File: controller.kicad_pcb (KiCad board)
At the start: 2 copper layers, 26.8 x 31.5 mm, 27 parts, among them J1 Conn_ST_STDC14, P1 USB_C_Plug_USB2.0, SW1 SW_Push, SW2 SW_Push, U1 STM32L476RGTx, U2 BD33FC0FP, U3 NUP2202

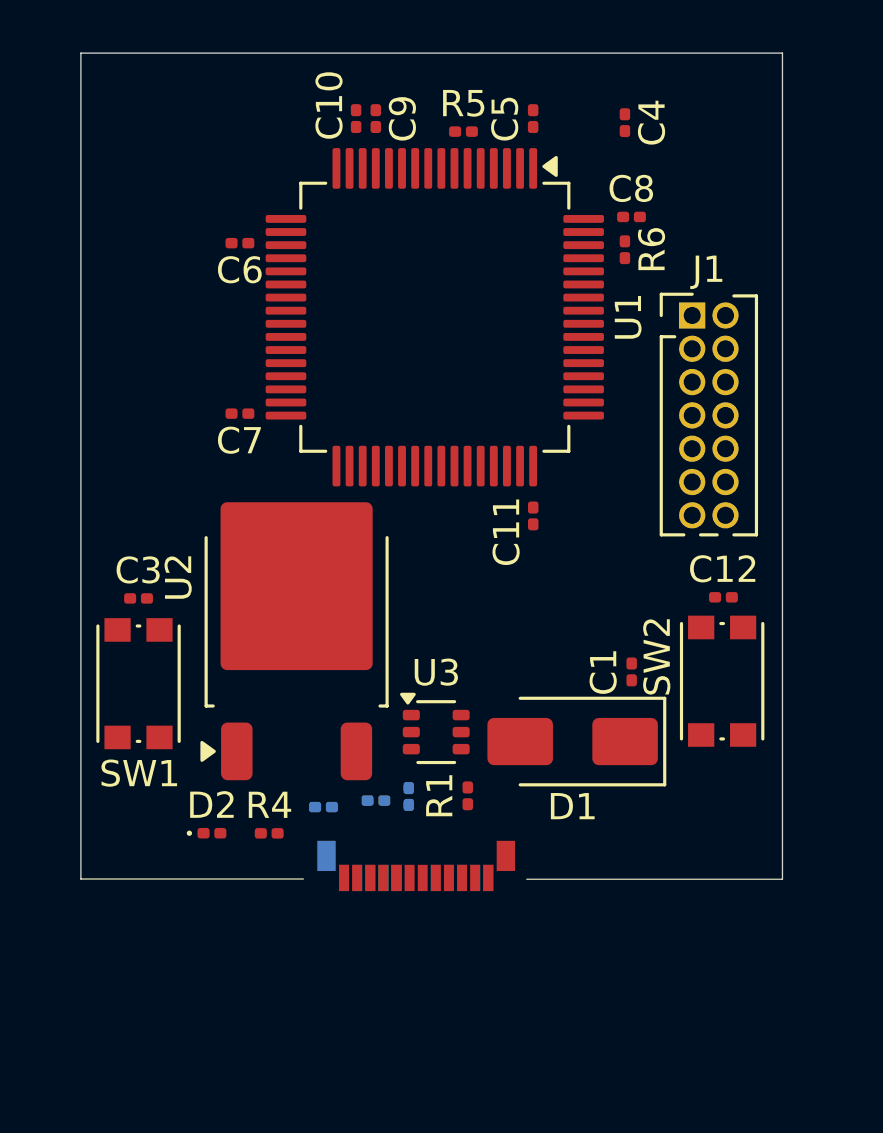
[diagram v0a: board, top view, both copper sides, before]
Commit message: initial ground/power routing
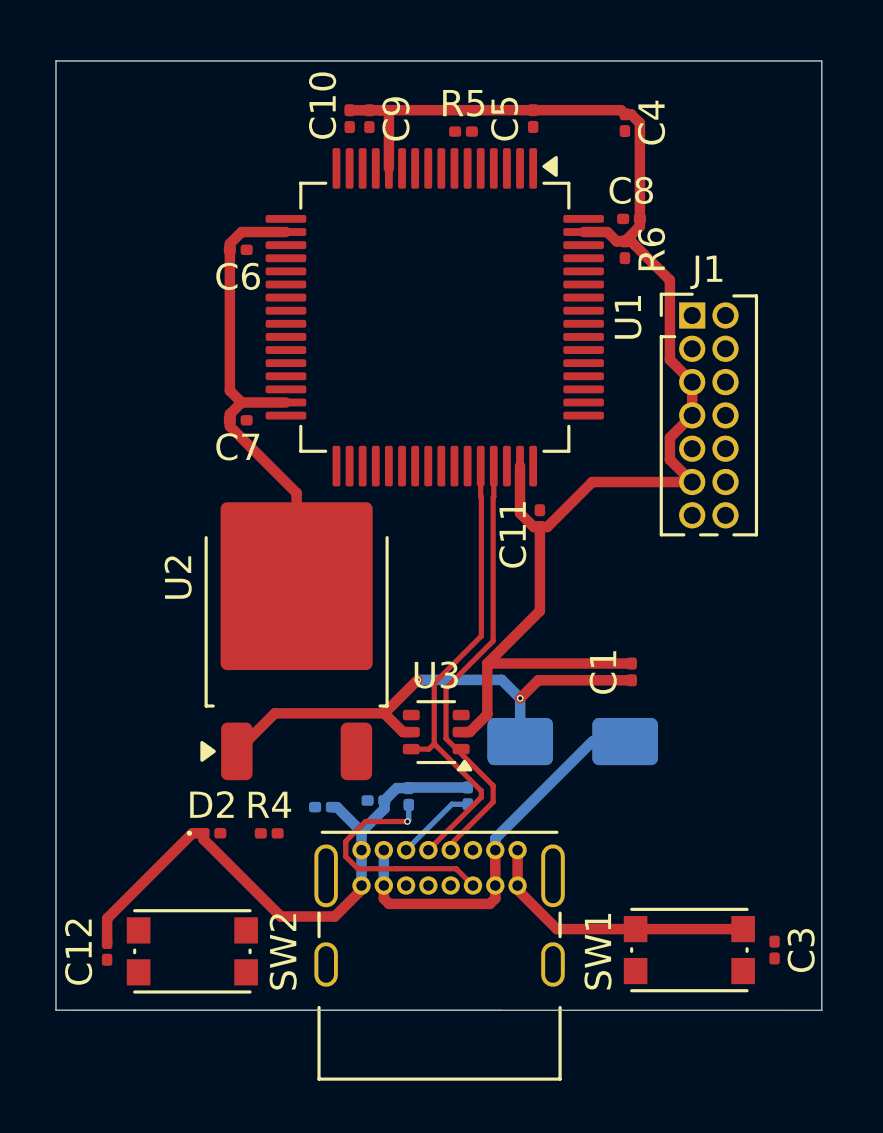
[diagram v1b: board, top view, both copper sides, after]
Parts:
- D1, R1: moved to B.Cu
- P1: footprint Connector_USB:USB_C_Plug_Molex_105444 -> Connector_USB:USB_C_Receptacle_GCT_USB4085
- moved C3 27.7 mm to (89.2, 79.7), turned to -90 degrees
- moved C12 27.1 mm to (63.8, 79.8), turned to 90 degrees
- moved SW1 23.3 mm to (86.0, 79.7), turned to 0 degrees
- moved SW2 22.7 mm to (67.0, 79.8), turned to 0 degrees
- moved P1 2.36 mm to (73.5, 75.9), turned to 0 degrees
- moved C11 0.27 mm to (80.2, 63.2)
- moved C6 0.26 mm to (68.8, 53.0)
- moved C7 0.26 mm to (68.8, 59.5)
- moved C10 0.24 mm to (73.0, 48.0)
- moved C9 0.24 mm to (73.8, 48.0)
- moved C8 0.08 mm to (83.7, 51.8)
- turned D1 to 0 degrees
- turned U3 to 180 degrees
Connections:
- net Net-(D1-A) renamed /VUSB
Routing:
- net GND: track 0.00 -> 106.8 mm
- net +5V: track 0.00 -> 19.7 mm, vias 0 -> 2
- net D+: track 0.00 -> 17.9 mm
- net D-: track 0.00 -> 16.8 mm
- net /VUSB: track 0.00 -> 15.0 mm
- net Net-(P1-VCONN): track 0.00 -> 9.21 mm, vias 0 -> 1
- net Net-(P1-CC): track 0.00 -> 3.07 mm
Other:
- board size 26.8 x 31.5 mm -> 29.2 x 36.2 mm

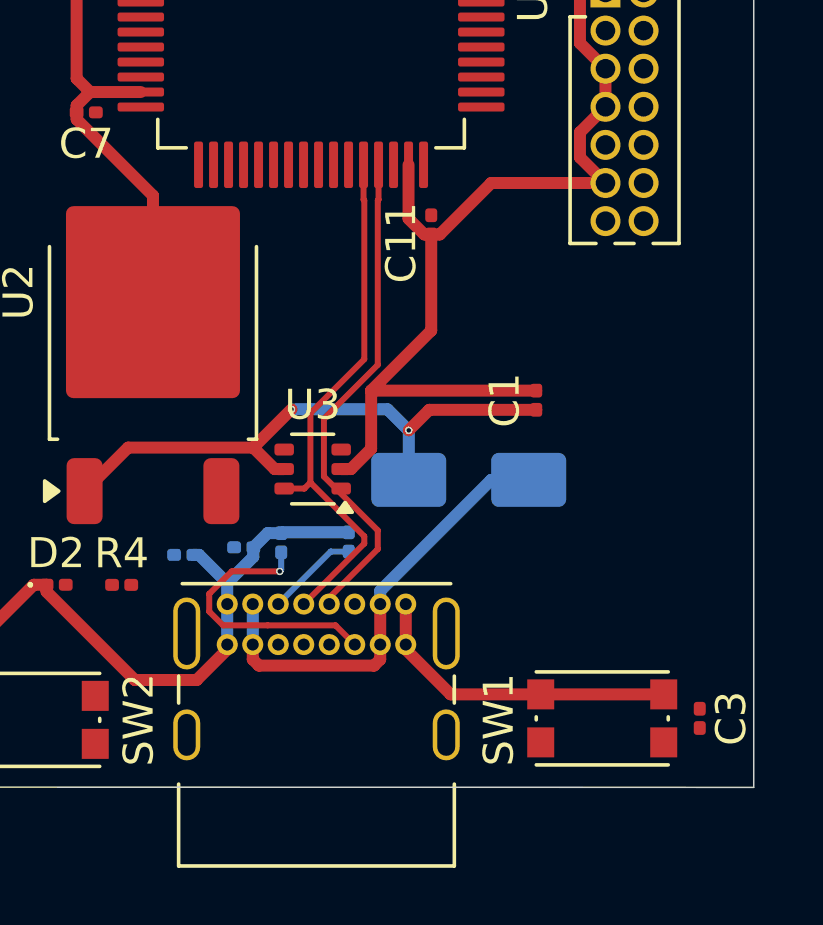
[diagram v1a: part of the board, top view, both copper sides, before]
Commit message: a bit more power routing
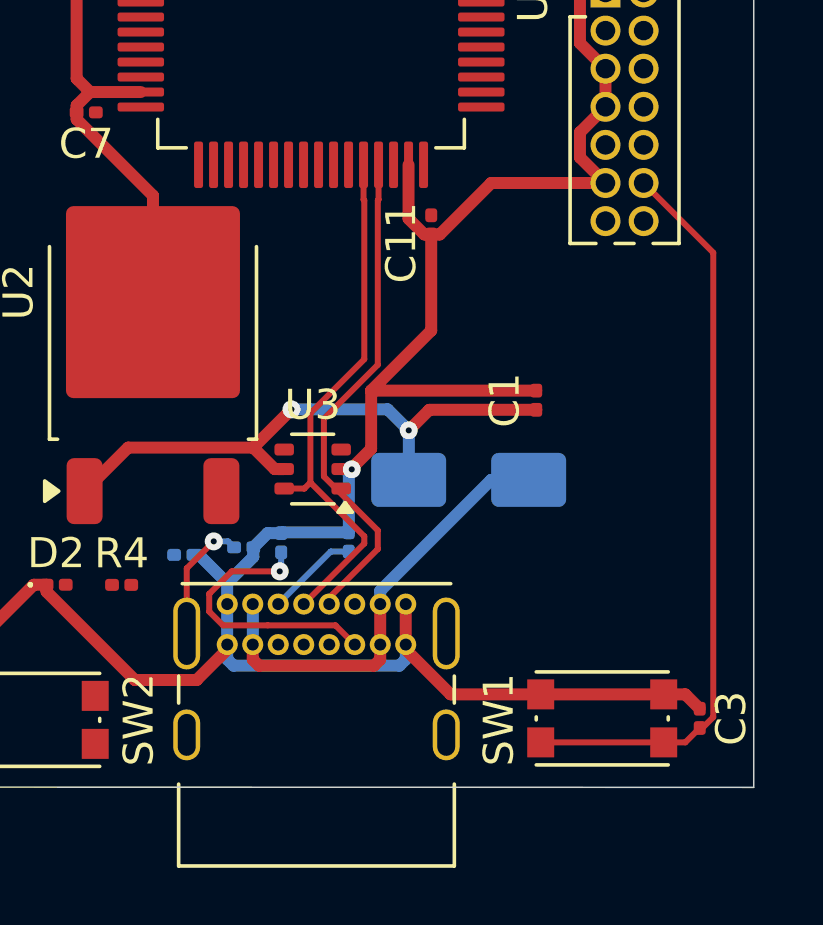
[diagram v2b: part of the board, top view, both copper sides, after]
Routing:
- net nRST: track 0.00 -> 24.9 mm
- net GND: track 106.8 -> 117.5 mm, vias 0 -> 1
- net Net-(P1-SHIELD): track 0.00 -> 4.21 mm, vias 0 -> 1
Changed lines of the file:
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@@
 		(tags "resistor")
 		(property "Reference" "R1"
-			(at 0 1.05 90)
+			(at -0.58 1.1 90)
 			(layer "B.SilkS")
 			(effects
@@
 	)
 	(via
-		(at 75.591369 69.4)
-		(size 0.25)
-		(drill 0.15)
+		(at 79.5 70.1)
+		(size 0.6)
+		(drill 0.2)
 		(layers "F.Cu" "B.Cu")
 		(net 1)
 	)
 	(via
-		(at 79.5 70.1)
-		(size 0.25)
-		(drill 0.15)
+		(at 75.591369 69.4)
+		(size 0.6)
+		(drill 0.2)
 		(layers "F.Cu" "B.Cu")
 		(net 1)
@@
 	)
 	(segment
+		(start 88.72 78.9)
+		(end 89.2 79.38)
+		(width 0.4)
+		(layer "F.Cu")
+		(net 2)
+	)
+	(segment
 		(start 80.53411 63.57)
 		(end 82.25 61.85411)
@@
 	)
 	(segment
+		(start 88 78.9)
+		(end 88.72 78.9)
+		(width 0.4)
+		(layer "F.Cu")
+		(net 2)
+	)
+	(segment
 		(start 68.43 52.769418)
 		(end 68.43 53)
@@
 		(net 2)
 	)
+	(via
+		(at 77.6 71.4)
+		(size 0.6)
+		(drill 0.2)
+		(layers "F.Cu" "B.Cu")
+		(net 2)
+	)
 	(segment
 		(start 72.512 74.25)
@@
 	)
 	(segment
+		(start 79.4 77.24)
+		(end 79.4 77.734974)
+		(width 0.4)
+		(layer "B.Cu")
+		(net 2)
+	)
+	(segment
+		(start 73.45 77.734974)
+		(end 73.45 77.24)
+		(width 0.4)
+		(layer "B.Cu")
+		(net 2)
+	)
+	(segment
 		(start 73.45 75.89)
 		(end 73.45 77.24)
@@
 	)
 	(segment
+		(start 73.656026 77.941)
+		(end 73.45 77.734974)
+		(width 0.4)
+		(layer "B.Cu")
+		(net 2)
+	)
+	(segment
+		(start 77.5 71.5)
+		(end 77.6 71.4)
+		(width 0.4)
+		(layer "B.Cu")
+		(net 2)
+	)
+	(segment
 		(start 74.32 74.318)
 		(end 74.32 74)
@@
 	(segment
 		(start 77.5 73.5)
+		(end 77.5 71.5)
+		(width 0.4)
+		(layer "B.Cu")
+		(net 2)
+	)
+	(segment
+		(start 77.5 73.5)
 		(end 75.275 73.5)
 		(width 0.4)
@@
 	)
 	(segment
+		(start 79.4 77.734974)
+		(end 79.193974 77.941)
+		(width 0.4)
+		(layer "B.Cu")
+		(net 2)
+	)
+	(segment
+		(start 79.193974 77.941)
+		(end 73.656026 77.941)
+		(width 0.4)
+		(layer "B.Cu")
+		(net 2)
+	)
+	(segment
 		(start 74.795 73.525)
 		(end 75.25 73.525)
@@
 	)
 	(segment
+		(start 89.651 79.65816)
+		(end 89.651 64.176401)
+		(width 0.2)
+		(layer "F.Cu")
+		(net 4)
+	)
+	(segment
+		(start 89.28916 80.02)
+		(end 89.651 79.65816)
+		(width 0.2)
+		(layer "F.Cu")
+		(net 4)
+	)
+	(segment
+		(start 89.2 80.02)
+		(end 89.28916 80.02)
+		(width 0.2)
+		(layer "F.Cu")
+		(net 4)
+	)
+	(segment
+		(start 89.651 64.176401)
+		(end 87.328709 61.85411)
+		(width 0.2)
+		(layer "F.Cu")
+		(net 4)
+	)
+	(segment
+		(start 88 80.5)
+		(end 83.9 80.5)
+		(width 0.2)
+		(layer "F.Cu")
+		(net 4)
+	)
+	(segment
+		(start 88 80.5)
+		(end 88.72 80.5)
+		(width 0.2)
+		(layer "F.Cu")
+		(net 4)
+	)
+	(segment
+		(start 88.72 80.5)
+		(end 89.2 80.02)
+		(width 0.2)
+		(layer "F.Cu")
+		(net 4)
+	)
+	(segment
 		(start 78.55 77.734974)
 		(end 78.55 77.24)
@@
 	)
 	(segment
+		(start 72.1 74.7)
+		(end 73 73.8)
+		(width 0.2)
+		(layer "F.Cu")
+		(net 18)
+	)
+	(segment
+		(start 72.1 76.87)
+		(end 72.1 74.7)
+		(width 0.2)
+		(layer "F.Cu")
+		(net 18)
+	)
+	(via
+		(at 73 73.8)
+		(size 0.6)
+		(drill 0.2)
+		(layers "F.Cu" "B.Cu")
+		(net 18)
+	)
+	(segment
+		(start 73.48 73.8)
+		(end 73.68 74)
+		(width 0.2)
+		(layer "B.Cu")
+		(net 18)
+	)
+	(segment
+		(start 73 73.8)
+		(end 73.48 73.8)
+		(width 0.2)
+		(layer "B.Cu")
+		(net 18)
+	)
+	(segment
 		(start 76.9 74.14)
 		(end 77.5 74.14)
@@
 	(via
 		(at 75.2 74.8)
-		(size 0.25)
-		(drill 0.15)
+		(size 0.6)
+		(drill 0.2)
 		(layers "F.Cu" "B.Cu")
 		(net 21)

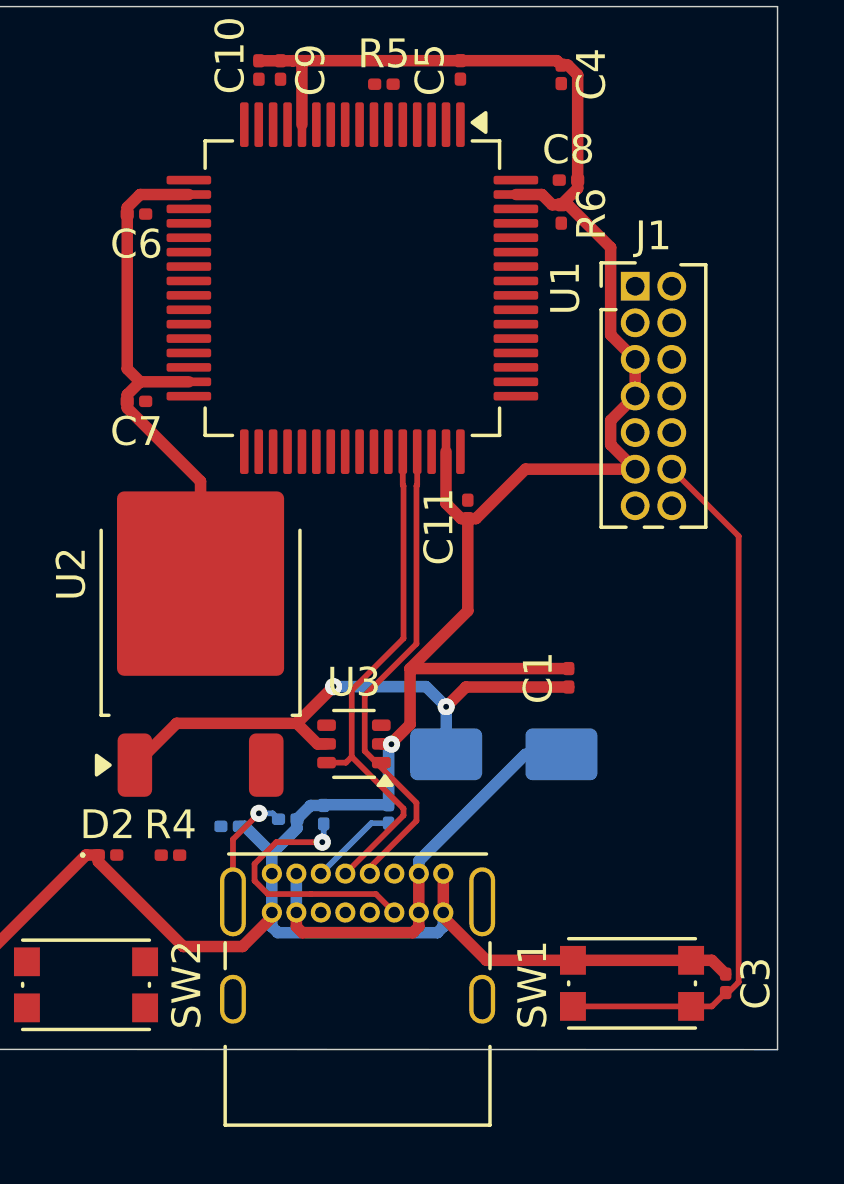
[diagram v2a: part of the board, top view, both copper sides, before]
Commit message: change to receptacle
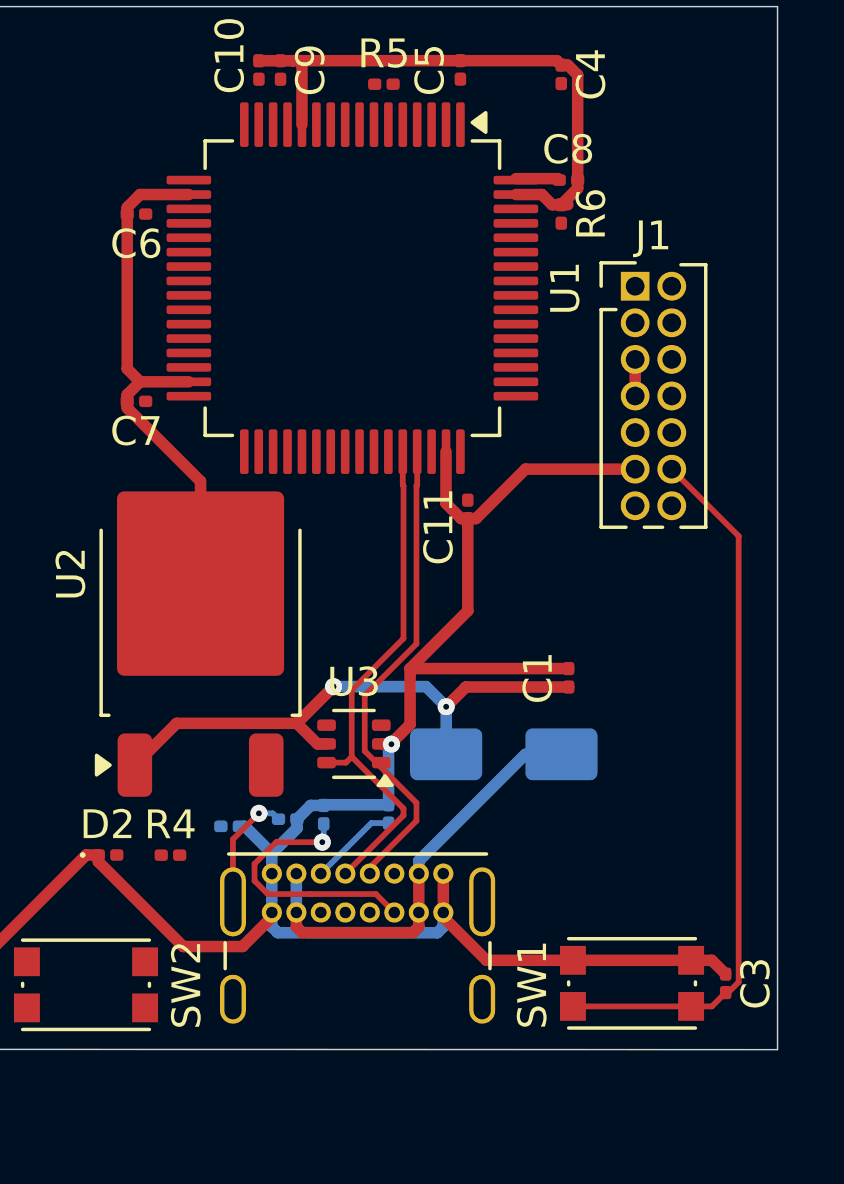
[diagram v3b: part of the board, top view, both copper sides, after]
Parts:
- removed P1: USB_C_Plug_USB2.0, Connector_USB:USB_C_Receptacle_GCT_USB4085
- added J2: USB_C_Receptacle_USB2.0_14P, Connector_USB:USB_C_Receptacle_GCT_USB4085, F.Cu at (73.5, 75.9)
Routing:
- net GND: track 117.5 -> 107.9 mm
- net +3.3V: track 0.00 -> 1.53 mm

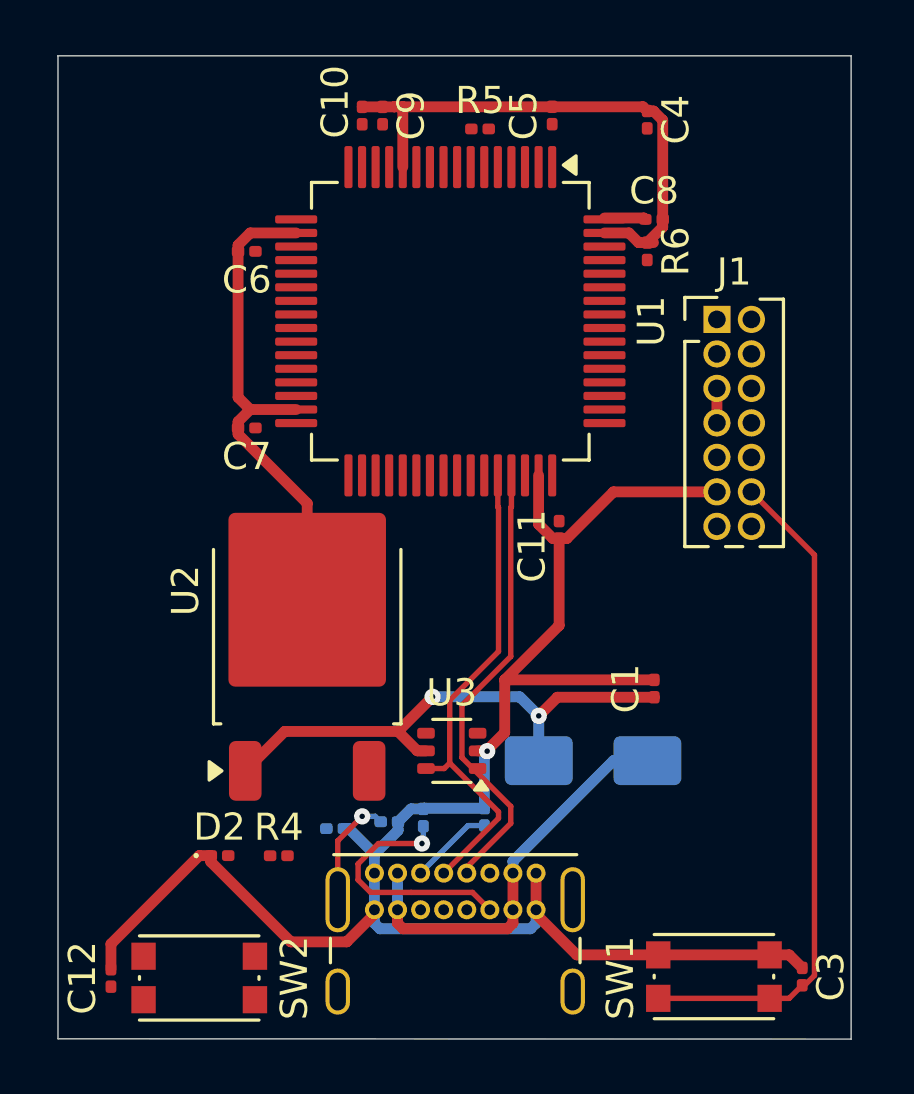
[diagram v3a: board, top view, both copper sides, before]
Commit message: fix some DRC checks
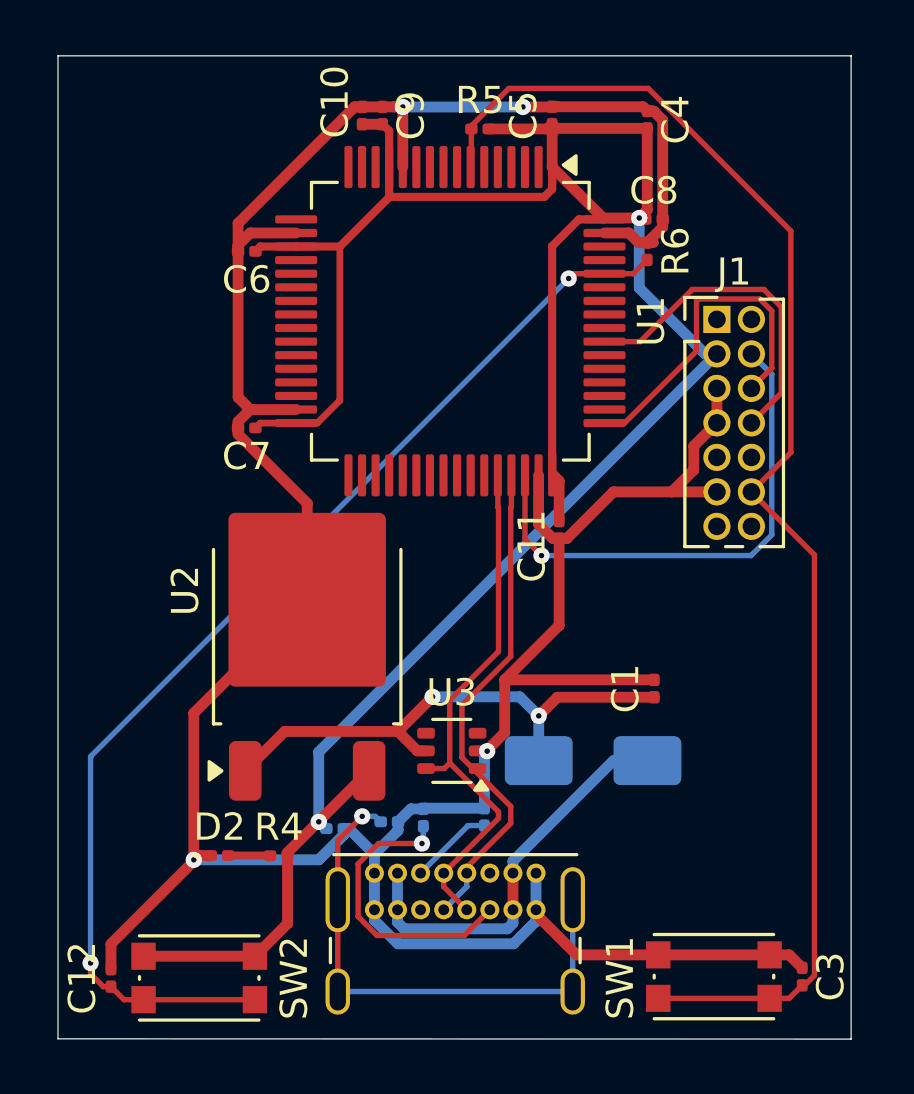
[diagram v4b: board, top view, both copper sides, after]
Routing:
- net +3.3V: track 1.53 -> 96.7 mm, vias 0 -> 2
- net BOOT0: track 0.00 -> 42.5 mm, vias 0 -> 2
- net nRST: track 24.9 -> 51.1 mm
- net GND: track 107.9 -> 128.4 mm, vias 1 -> 4
- net SWDIO: track 0.00 -> 19.0 mm, vias 0 -> 1
- net Net-(J2-SHIELD): track 4.21 -> 19.6 mm
- net SWCLK: track 0.00 -> 12.5 mm
- net SWO: track 0.00 -> 12.3 mm
- net D-: track 16.8 -> 18.5 mm
- net D+: track 17.9 -> 19.6 mm
- net Net-(J2-CC2): track 9.21 -> 10.8 mm
- net Net-(D2-A): track 0.00 -> 1.55 mm
